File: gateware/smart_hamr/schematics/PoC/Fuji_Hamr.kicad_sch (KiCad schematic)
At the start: 7 parts, among them J1 SD Card - HW-125, J2 Conn_01x11_Socket, U2 ESP32-DevKitC

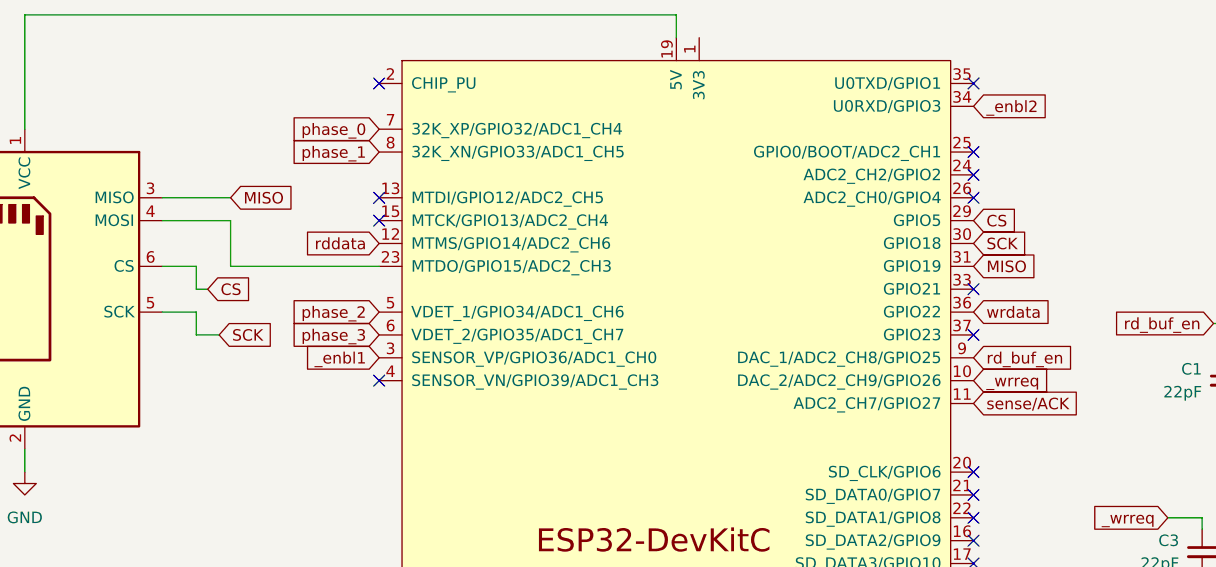
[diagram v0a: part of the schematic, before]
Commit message: Fix MOSI Line in POC
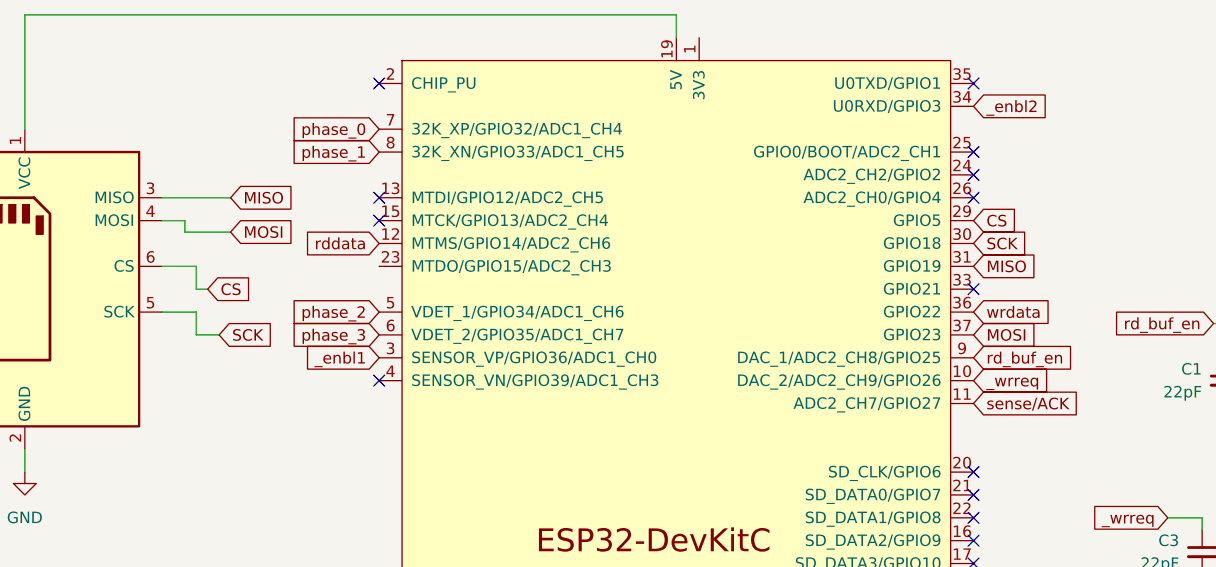
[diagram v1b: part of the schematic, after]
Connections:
- net at U2.23 (MTDO/GPIO15/ADC2_CH3): no longer J1.4 (MOSI)
- net MOSI: now reaches U2.37 (GPIO23)
- net MOSI: now also J1.4 (MOSI)
- no-connect marks 18 -> 17
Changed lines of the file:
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@@
-	)
-	(no_connect
-		(at 148.59 60.96)
 	)
 	(no_connect
@@
 	(wire
 		(pts
-			(xy 66.04 48.26) (xy 66.04 53.34)
-		)
-		(stroke
-			(width 0)
-			(type default)
-		)
-	)
-	(wire
-		(pts
 			(xy 62.23 55.88) (xy 62.23 53.34)
 		)
@@
 	(wire
 		(pts
+			(xy 60.96 48.26) (xy 60.96 49.53)
+		)
+		(stroke
+			(width 0)
+			(type default)
+		)
+	)
+	(wire
+		(pts
 			(xy 43.18 25.4) (xy 115.57 25.4)
 		)
@@
 	(wire
 		(pts
+			(xy 58.42 48.26) (xy 60.96 48.26)
+		)
+		(stroke
+			(width 0)
+			(type default)
+		)
+	)
+	(wire
+		(pts
 			(xy 173.99 81.28) (xy 173.99 82.55)
 		)
@@
 	(wire
 		(pts
+			(xy 60.96 49.53) (xy 66.04 49.53)
+		)
+		(stroke
+			(width 0)
+			(type default)
+		)
+	)
+	(wire
+		(pts
 			(xy 182.88 90.17) (xy 194.31 90.17)
 		)
@@
 	(wire
 		(pts
-			(xy 58.42 48.26) (xy 66.04 48.26)
-		)
-		(stroke
-			(width 0)
-			(type default)
-		)
-	)
-	(wire
-		(pts
 			(xy 58.42 58.42) (xy 62.23 58.42)
 		)
@@
 	(wire
 		(pts
-			(xy 66.04 53.34) (xy 82.55 53.34)
-		)
-		(stroke
-			(width 0)
-			(type default)
-		)
-	)
-	(wire
-		(pts
 			(xy 170.18 81.28) (xy 173.99 81.28)
 		)
@@
 		)
 	)
+	(global_label "MOSI"
+		(shape input)
+		(at 148.59 60.96 0)
+		(fields_autoplaced yes)
+		(effects
+			(font
+				(size 1.27 1.27)
+			)
+			(justify left)
+		)
+		(property "Intersheetrefs" "${INTERSHEET_REFS}"
+			(at 156.1714 60.96 0)
+			(effects
+				(font
+					(size 1.27 1.27)
+				)
+				(justify left)
+				(hide yes)
+			)
+		)
+	)
 	(global_label "_enbl1"
 		(shape input)
@@
 				(hide yes)
 			)
+		)
+	)
+	(global_label "MOSI"
+		(shape input)
+		(at 66.04 49.53 0)
+		(fields_autoplaced yes)
+		(effects
+			(font
+				(size 1.27 1.27)
+			)
+			(justify left)
+		)
+		(property "Intersheetrefs" "${INTERSHEET_REFS}"
+			(at 73.6214 49.53 0)
+			(effects
+				(font
+					(size 1.27 1.27)
+				)
+				(justify left)
+				(hide yes)
+			)
